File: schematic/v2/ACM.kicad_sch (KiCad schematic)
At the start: 12 parts, among them J1 FPGA I/O, J2 FPGA I/O, J8 FPGA I/O, J9 FPGA I/O

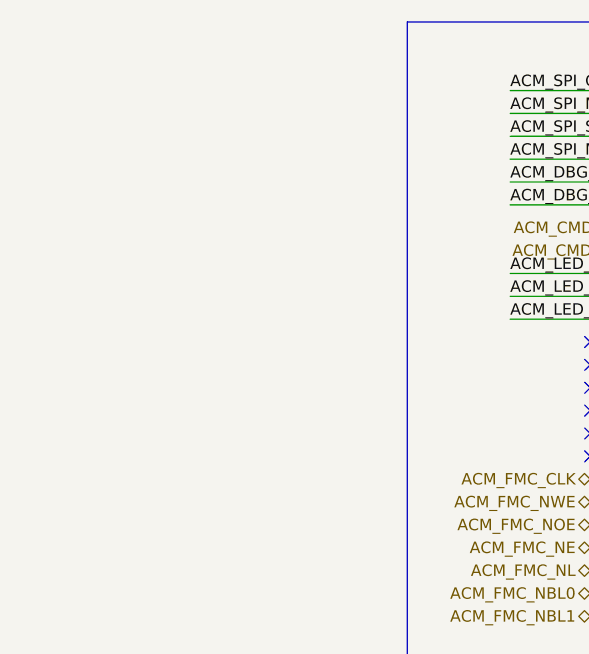
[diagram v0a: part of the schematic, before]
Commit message: moving AAM -> APM. creatint some abstraction like stuff
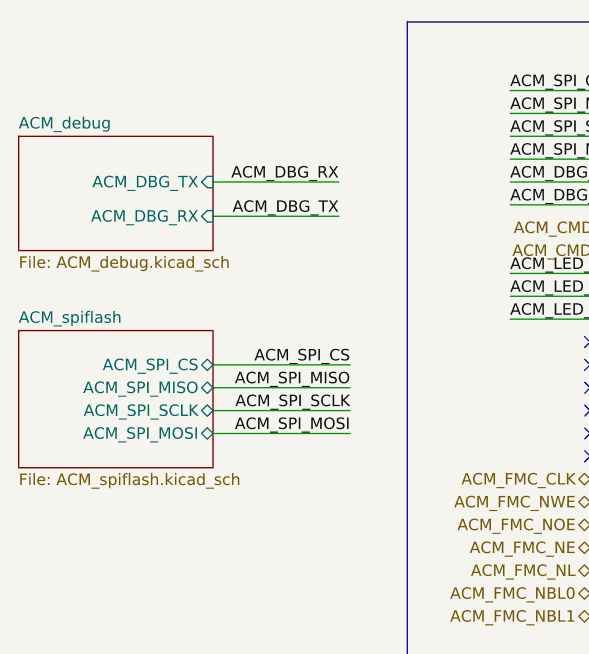
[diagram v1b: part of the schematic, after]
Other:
- added sheet ACM_debug (ACM_debug.kicad_sch)
- added sheet ACM_spiflash (ACM_spiflash.kicad_sch)

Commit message: no errors in the ERC!
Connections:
- net at J9.17 (Pin_17): now also J2.17 (Pin_17)
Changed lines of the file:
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@@
 	)
 	(junction
+		(at 168.91 71.12)
+		(diameter 0)
+		(color 0 0 0 0)
+	)
+	(junction
 		(at 119.38 40.64)
 		(diameter 0)
@@
 	)
 	(junction
+		(at 196.85 73.66)
+		(diameter 0)
+		(color 0 0 0 0)
+	)
+	(junction
 		(at 196.85 88.9)
 		(diameter 0)
@@
 	(wire
 		(pts
+			(xy 196.85 74.93) (xy 196.85 73.66)
+		)
+		(stroke
+			(width 0)
+			(type default)
+		)
+	)
+	(wire
+		(pts
 			(xy 104.14 55.88) (xy 119.38 55.88)
 		)
@@
 	(wire
 		(pts
+			(xy 161.29 71.12) (xy 168.91 71.12)
+		)
+		(stroke
+			(width 0)
+			(type default)
+		)
+	)
+	(wire
+		(pts
 			(xy 119.38 38.1) (xy 127 38.1)
 		)
@@
 					(unit 1)
 				)
+			)
+		)
+	)
+	(symbol
+		(lib_id "power:PWR_FLAG")
+		(at 196.85 74.93 180)
+		(unit 1)
+		(exclude_from_sim no)
+		(in_bom yes)
+		(on_board yes)
+		(dnp no)
+		(fields_autoplaced yes)
+		(property "Reference" "#FLG01"
+			(at 196.85 76.835 0)
+			(effects
+				(font
+					(size 1.27 1.27)
+				)
+				(hide yes)
+			)
+		)
+		(property "Value" "PWR_FLAG"
+			(at 199.39 76.1999 0)
+			(effects
+				(font
+					(size 1.27 1.27)
+				)
+				(justify right)
+			)
+		)
+		(property "Footprint" ""
+			(at 196.85 74.93 0)
+			(effects
+				(font
+					(size 1.27 1.27)
+				)
+				(hide yes)
+			)
+		)
+		(property "Datasheet" "~"
+			(at 196.85 74.93 0)
+			(effects
+				(font
+					(size 1.27 1.27)
+				)
+				(hide yes)
+			)
+		)
+		(property "Description" "Special symbol for telling ERC where power comes from"
+			(at 196.85 74.93 0)
+			(effects
+				(font
+					(size 1.27 1.27)
+				)
+				(hide yes)
+			)
+		)
+		(pin "1"
+		)
+		(instances
+			(project "signalmesh"
+				(path "/fe7b15e9-f0ed-4338-9f03-dd7651dace13/c5977503-4ab2-47b6-bfc3-7f974cfcf6ea"
+					(reference "#FLG01")
+					(unit 1)
+				)

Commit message: time to start routing?
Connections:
- net ACM_VDD is gone; now on net 5V_ACM: R34.2
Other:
- removed sheet ACM_debug
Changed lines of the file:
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@@
 	(wire
 		(pts
-			(xy 85.09 44.45) (xy 71.12 44.45)
-		)
-		(stroke
-			(width 0)
-			(type default)
-		)
-	)
-	(wire
-		(pts
 			(xy 173.99 30.48) (xy 168.91 30.48)
 		)
@@
 	(wire
 		(pts
-			(xy 104.14 40.64) (xy 119.38 40.64)
+			(xy 118.11 40.64) (xy 119.38 40.64)
 		)
 		(stroke
@@
 	(wire
 		(pts
-			(xy 85.09 40.64) (xy 71.12 40.64)
-		)
-		(stroke
-			(width 0)
-			(type default)
-		)
-	)
-	(wire
-		(pts
 			(xy 119.38 76.2) (xy 127 76.2)
 		)
@@
 	(wire
 		(pts
-			(xy 104.14 43.18) (xy 119.38 43.18)
+			(xy 118.11 43.18) (xy 119.38 43.18)
 		)
 		(stroke
@@
 	(wire
 		(pts
+			(xy 196.85 73.66) (xy 199.39 73.66)
+		)
+		(stroke
+			(width 0)
+			(type default)
+		)
+	)
+	(wire
+		(pts
 			(xy 196.85 88.9) (xy 196.85 87.63)
 		)
@@
 		)
 	)
-	(label "ACM_DBG_RX"
-		(at 85.09 40.64 180)
-		(effects
-			(font
-				(size 1.27 1.27)
-			)
-			(justify right bottom)
-		)
-	)
 	(label "ACM_SPI_SCLK"
 		(at 86.36 66.04 180)
@@
 		)
 	)
-	(label "ACM_DBG_TX"
-		(at 85.09 44.45 180)
-		(effects
-			(font
-				(size 1.27 1.27)
-			)
-			(justify right bottom)
-		)
-	)
 	(label "ACM_SPI_MOSI"
 		(at 86.36 68.58 180)
@@
 		)
 	)
-	(label "ACM_DBG_TX"
-		(at 104.14 40.64 0)
-		(effects
-			(font
-				(size 1.27 1.27)
-			)
-			(justify left bottom)
-		)
-	)
 	(label "ACM_SPI_MOSI"
 		(at 104.14 33.02 0)
@@
 		)
 	)
-	(label "ACM_DBG_RX"
-		(at 104.14 43.18 0)
-		(effects
-			(font
-				(size 1.27 1.27)
-			)
-			(justify left bottom)
-		)
-	)
 	(global_label "ACM_VDD"
 		(shape input)
@@
 		)
 	)
+	(hierarchical_label "ACM_DBG_TX"
+		(shape output)
+		(at 118.11 40.64 180)
+		(effects
+			(font
+				(size 1.27 1.27)
+			)
+			(justify right)
+		)
+	)
 	(hierarchical_label "ACM_FMC_D14"
 		(shape bidirectional)
@@
 		)
 	)
+	(hierarchical_label "ACM_DBG_RX"
+		(shape input)
+		(at 118.11 43.18 180)
+		(effects
+			(font
+				(size 1.27 1.27)
+			)
+			(justify right)
+		)
+	)
 	(hierarchical_label "ACM_FMC_D9"
 		(shape bidirectional)
@@
 		)
 	)
+	(hierarchical_label "ACM_VDD"
+		(shape output)
+		(at 199.39 73.66 0)
+		(effects
+			(font
+				(size 1.27 1.27)
+			)
+			(justify left)
+		)
+	)
 	(hierarchical_label "ACM_FMC_NWE"
 		(shape bidirectional)
@@
 				)
 			)
-		)
-	)
-	(sheet
-		(at 49.53 35.56)
-		(size 21.59 12.7)
-		(exclude_from_sim no)
-		(in_bom yes)
-		(on_board yes)
-		(dnp no)
-		(fields_autoplaced yes)
-		(stroke
-			(width 0.1524)
-			(type solid)
-		)
-		(fill
-			(color 0 0 0 0.0000)
-		)
-		(property "Sheetname" "ACM_debug"
-			(at 49.53 34.8484 0)
-			(effects
-				(font
-					(size 1.27 1.27)
-				)
-				(justify left bottom)
-			)
-		)
-		(property "Sheetfile" "ACM_debug.kicad_sch"
-			(at 49.53 48.8446 0)
-			(effects
-				(font
-					(size 1.27 1.27)
-				)
-				(justify left top)
-			)
-		)
-		(pin "ACM_DBG_RX" input
-			(at 71.12 44.45 0)
-			(effects
-				(font
-					(size 1.27 1.27)
-				)
-				(justify right)
-			)
-		)
-		(pin "ACM_DBG_TX" input
-			(at 71.12 40.64 0)
-			(effects
-				(font
-					(size 1.27 1.27)
-				)
-				(justify right)
-			)
-		)
-		(instances
-			(project "signalmesh"
-				(path "/fe7b15e9-f0ed-4338-9f03-dd7651dace13/c5977503-4ab2-47b6-bfc3-7f974cfcf6ea"
-					(page "10")
-				)
-			)
